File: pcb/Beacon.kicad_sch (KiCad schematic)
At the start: 0 parts

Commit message: Set up schematic with Seeed XIAO and connector
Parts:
- added J1: PN532 NFC Module, symbol Connector:Conn_01x04_Pin
- added U1: XIAO-nRF52840-DIP, MCU_SEEED_XIAO_Series:XIAO-nRF52840-DIP, symbol Seeed Studio:XIAO-nRF52840-DIP
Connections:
- new net +5V: U1.14 (5V)
- new net GND: U1.13 (GND)

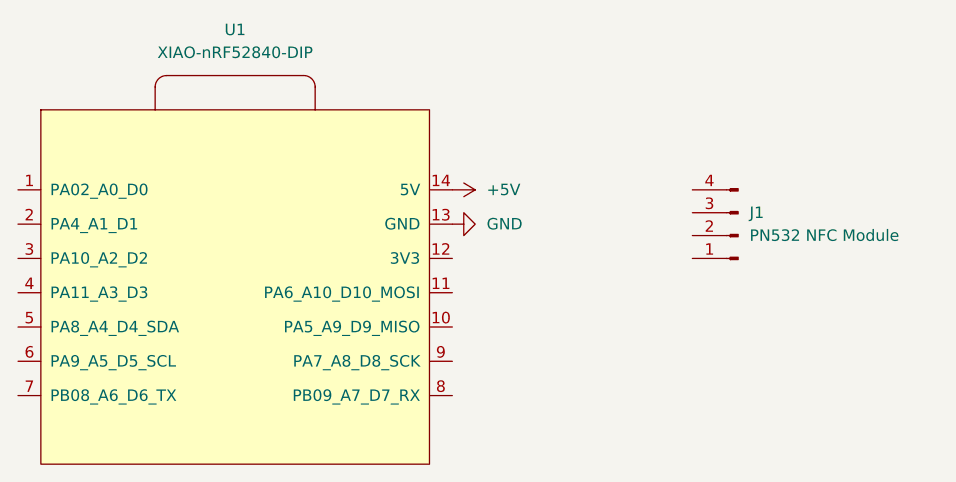
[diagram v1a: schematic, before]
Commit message: Change XIAO to RP2040
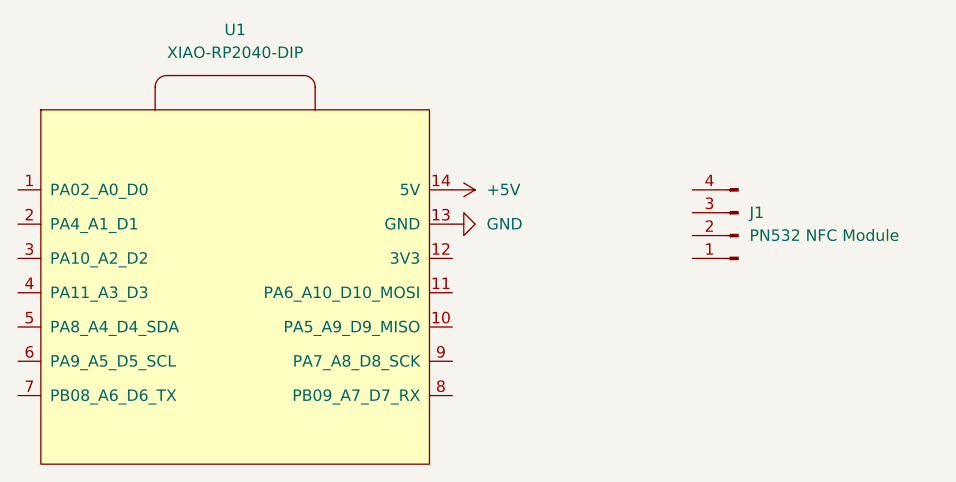
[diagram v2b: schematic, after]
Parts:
- removed U1: XIAO-nRF52840-DIP, MCU_SEEED_XIAO_Series:XIAO-nRF52840-DIP, symbol Seeed Studio:XIAO-nRF52840-DIP
- added U1: XIAO-RP2040-DIP, MCU_SEEED_XIAO_Series:XIAO-RP2040-DIP, symbol Seeed Studio:XIAO-RP2040-DIP
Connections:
- net +5V: now also U1.14 (5V)
- net GND: now also U1.13 (GND)
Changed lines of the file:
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@@
 	(paper "A4")
 	(symbol
-		(lib_id "Seeed Studio:XIAO-nRF52840-DIP")
+		(lib_id "Seeed Studio:XIAO-RP2040-DIP")
 		(at 129.54 100.33 0)
 		(unit 1)
@@
 			)
 		)
-		(property "Value" "XIAO-nRF52840-DIP"
+		(property "Value" "XIAO-RP2040-DIP"
 			(at 129.54 73.66 0)
 			(effects
@@
 			)
 		)
-		(property "Footprint" "MCU_SEEED_XIAO_Series:XIAO-nRF52840-DIP"
-			(at 129.54 123.698 0)
+		(property "Footprint" "MCU_SEEED_XIAO_Series:XIAO-RP2040-DIP"
+			(at 128.524 123.444 0)
 			(effects
 				(font
@@
 			)
 		)
-		(pin "8"
+		(pin "1"
 		)
-		(pin "6"
-		)
-		(pin "5"
+		(pin "2"
 		)
 		(pin "4"
-		)
-		(pin "9"
-		)
-		(pin "10"
 		)
 		(pin "3"
@@
 		(pin "14"
 		)
+		(pin "5"
+		)
+		(pin "11"
+		)
+		(pin "6"
+		)
+		(pin "10"
+		)
 		(pin "13"
 		)
 		(pin "12"
 		)
-		(pin "2"
+		(pin "9"
 		)
-		(pin "1"
-		)
-		(pin "11"
+		(pin "8"
 		)
 		(instances
